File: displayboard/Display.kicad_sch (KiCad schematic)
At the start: 15 parts, among them Q1401 NPN, X1401 Touch, X1402 Display, X1403 External

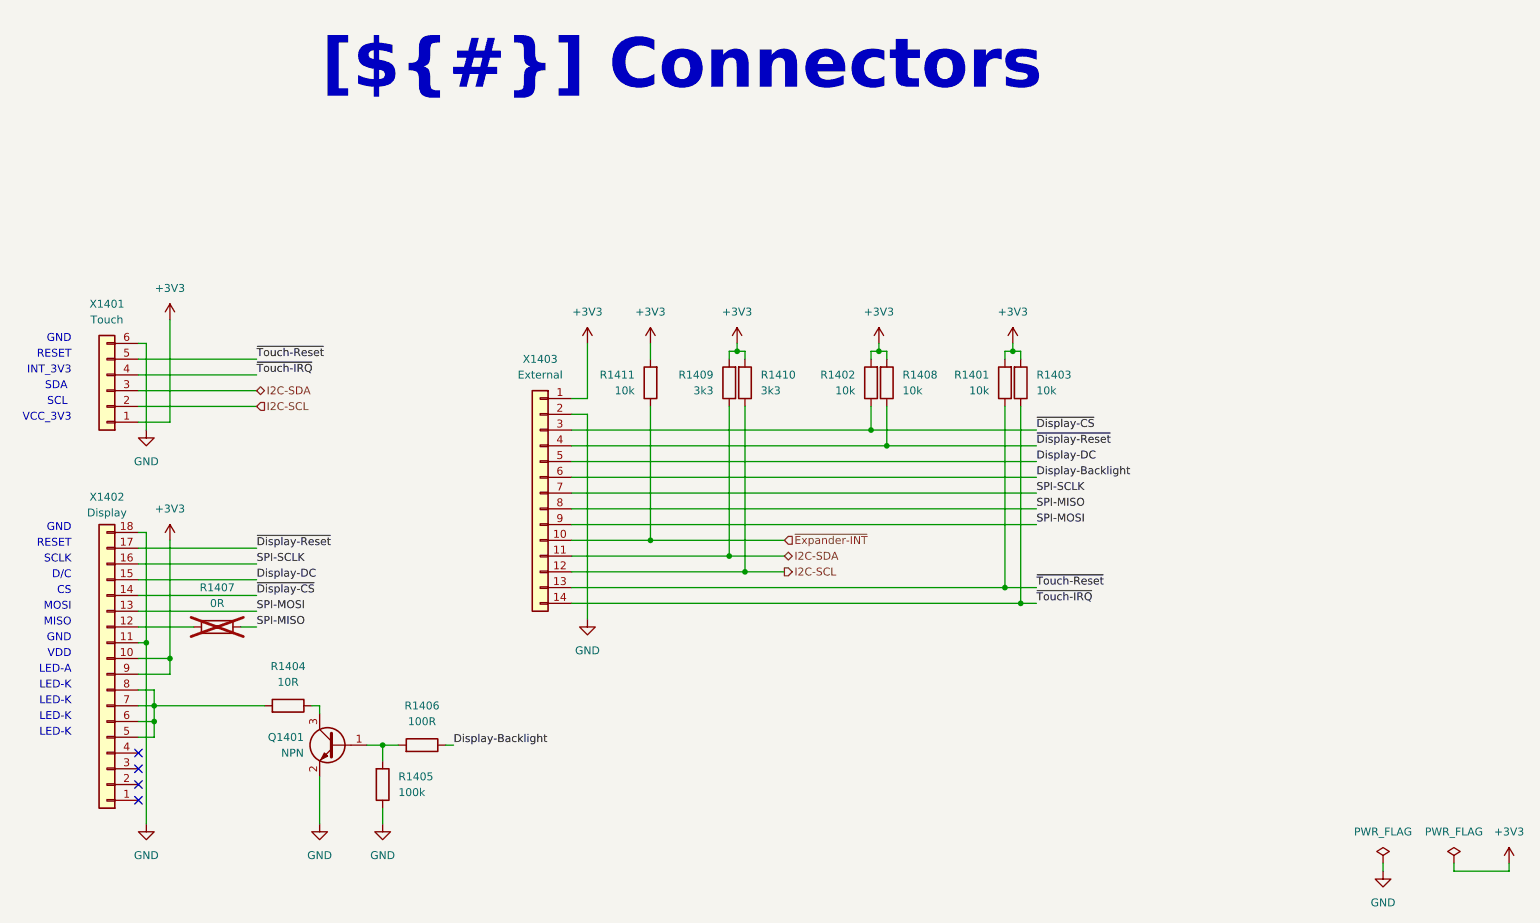
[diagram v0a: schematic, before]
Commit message: Remove old production files, add cutout for the programming cable, add connector for mainboard cable
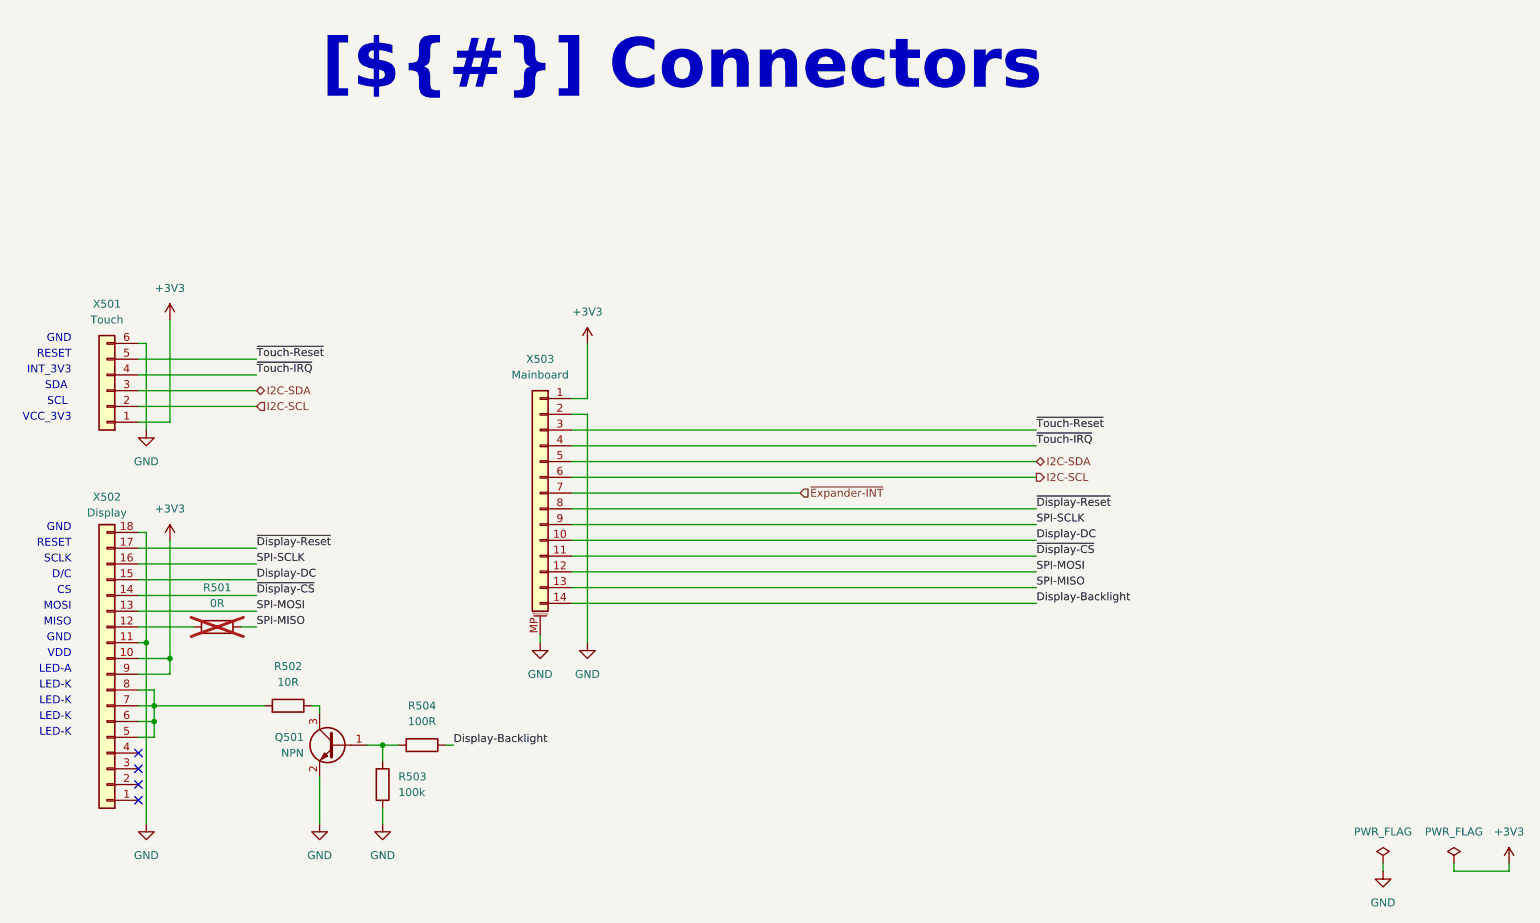
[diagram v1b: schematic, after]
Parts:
- removed R1401, R1402, R1403, R1408, R1411: 10k, Resistor_SMD:R_0805_2012Metric, symbol Device:R
- removed R1409, R1410: 3k3, Resistor_SMD:R_0805_2012Metric, symbol Device:R
- removed X1403: External, Connector_PinHeader_2.54mm:PinHeader_1x14_P2.54mm_Vertical, symbol Connector_Generic:Conn_01x14
- added X503: Mainboard, Connector_FFC-FPC:Amphenol_F32R-1A7x1-11014_1x14-1MP_P0.5mm_Horizontal, symbol Connector_Generic_MountingPin:Conn_01x14_MountingPin
- renumbered Q1401 to Q501, R1407 to R501, R1404 to R502, R1405 to R503, R1406 to R504, X1401 to X501, X1402 to X502
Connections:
- net +3V3: now also X503.1 (Pin_1)
- net Display-Backlight: now also X503.14 (Pin_14)
- net Display-DC: now also X503.10 (Pin_10)
- net GND: now also X503.2 (Pin_2), X503.MP (MountPin)
- net I2C-SCL: now also X503.6 (Pin_6)
- net I2C-SDA: now also X503.5 (Pin_5)
- net SPI-MISO: now also X503.13 (Pin_13)
- net SPI-MOSI: now also X503.12 (Pin_12)
- net SPI-SCLK: now also X503.9 (Pin_9)
- net ~{Display-CS}: now also X503.11 (Pin_11)
- net ~{Display-Reset}: now also X503.8 (Pin_8)
- net ~{Expander-INT}: now also X503.7 (Pin_7)
- net ~{Touch-IRQ}: now also X503.4 (Pin_4)
- net ~{Touch-Reset}: now also X503.3 (Pin_3)
